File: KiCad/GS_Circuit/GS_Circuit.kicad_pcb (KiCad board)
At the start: 2 copper layers, 88.9 x 76.2 mm, 17 parts, among them J1 AVR-ISP-6, SW1 SW_Push, SW2 SW_SPST, U2 ATtiny85V-10P

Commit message: Loose Saves
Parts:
- BT1: footprint Battery:BatteryHolder_TruPower_BH-331P_3xAA -> GS_Parts:BatteryHolder_Keystone_2464
- C1: value C -> .1 uf
- D1, D2: value LED, TLHG4600, TLHY4600, TLHY4600, TLHF4601 -> LED, QBL8XX60Y Series; footprint LED_THT:LED_D3.0mm -> GS_Parts:LED_D5.0mm
- R1, R2: value R_US -> 91 Ohms
- S1: footprint GS_Parts:TEPT4400 -> GS_Parts:THT_TEPT4400
- moved S1 55.8 mm to (68.2, 26.5)
- moved R4 11.4 mm to (64.4, 40.4)
- moved D2 4.91 mm to (91.9, 60.1)
- moved D1 3.94 mm to (25.8, 60.0)
- moved R3 3.18 mm to (74.5, 34.1)
- moved C1 0.35 mm to (48.1, 26.1)

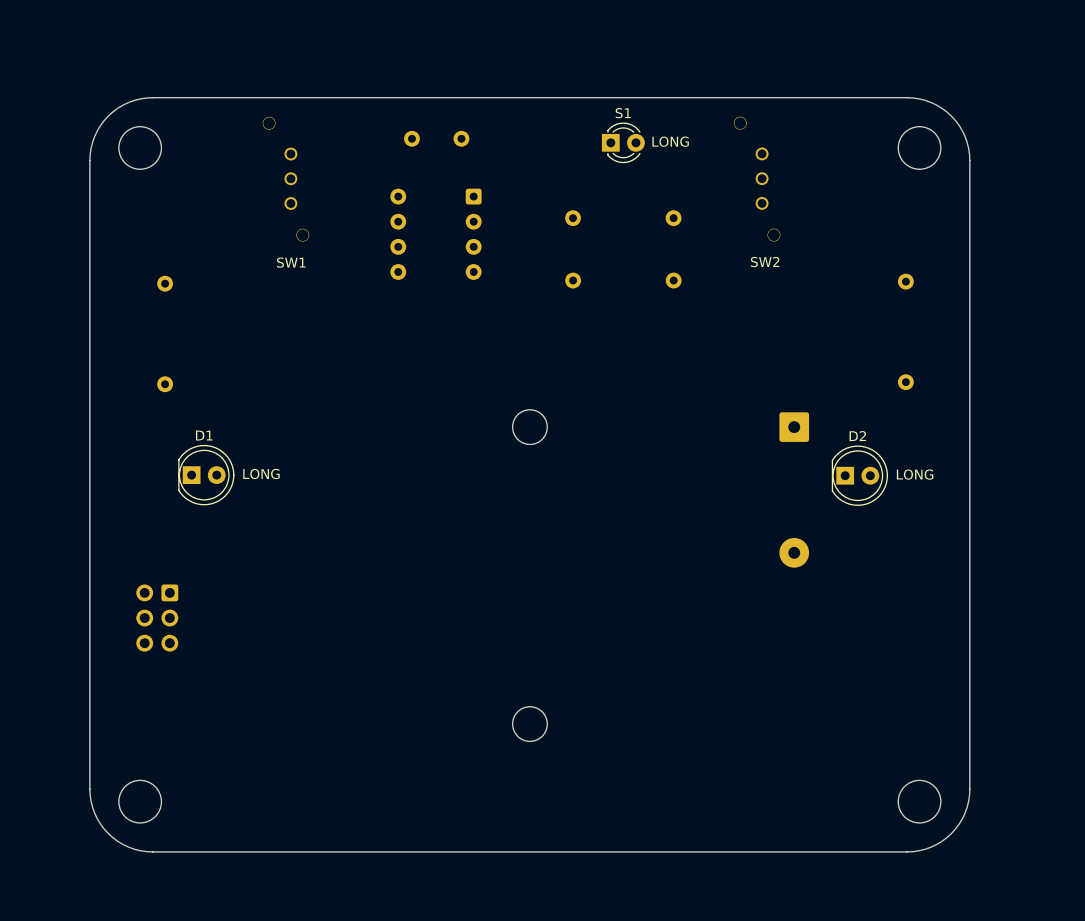
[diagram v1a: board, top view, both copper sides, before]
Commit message: MD E Feeback 3
Moved Lights
Horizontal/Vertical Wiring
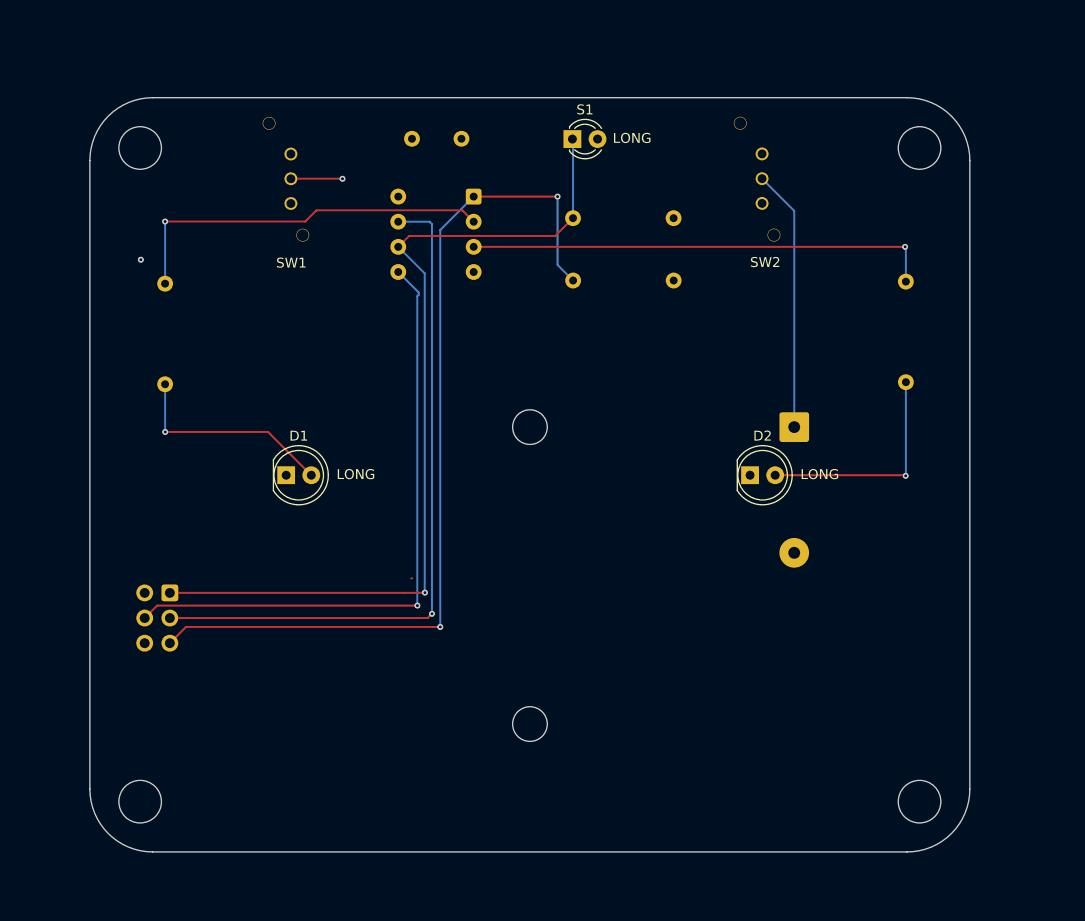
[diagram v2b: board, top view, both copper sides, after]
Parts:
- moved D2 9.62 mm to (82.2, 60.0)
- moved D1 9.55 mm to (35.4, 60.0)
- moved S1 3.90 mm to (64.3, 26.1)
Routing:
- net /~{RST}: track 0.00 -> 90.5 mm, vias 0 -> 2
- net /MISO: track 0.00 -> 88.7 mm, vias 0 -> 1
- net /SCK: track 0.00 -> 69.5 mm, vias 0 -> 1
- net /MOSI: track 0.00 -> 67.9 mm, vias 0 -> 3
- net Net-(U2-XTAL2/PB4): track 0.00 -> 47.1 mm, vias 0 -> 1
- net Net-(U2-XTAL1/PB3): track 0.00 -> 38.6 mm, vias 0 -> 1
- net Net-(BT1-+): track 0.00 -> 26.4 mm
- net Net-(D2-A): track 0.00 -> 22.7 mm, vias 0 -> 1
- net Net-(D1-A): track 0.00 -> 21.4 mm, vias 0 -> 1

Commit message: Wiring
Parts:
- moved R4 6.31 mm to (64.3, 34.1)
- moved R3 6.29 mm to (74.5, 40.4)
- moved R2 5.06 mm to (97.5, 55.7)
- moved R1 4.66 mm to (23.1, 55.5)
- moved D2 1.65 mm to (80.6, 60.0)
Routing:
- net /MOSI: track 67.9 -> 82.9 mm
- net /MISO: track 88.7 -> 96.8 mm
- net /~{RST}: track 90.5 -> 83.8 mm, vias 2 -> 1
- net Net-(D2-A): track 22.7 -> 16.1 mm, vias 1 -> 0
- net Net-(U2-XTAL2/PB4): track 47.1 -> 53.0 mm
- net Net-(D1-A): track 21.4 -> 16.7 mm
- net Net-(U2-XTAL1/PB3): track 38.6 -> 40.9 mm
- added copper zone on B.Cu, net GND
- added copper zone on F.Cu, net VCC
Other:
- board text added: "GS_NIGHT_LIGHT_V1"

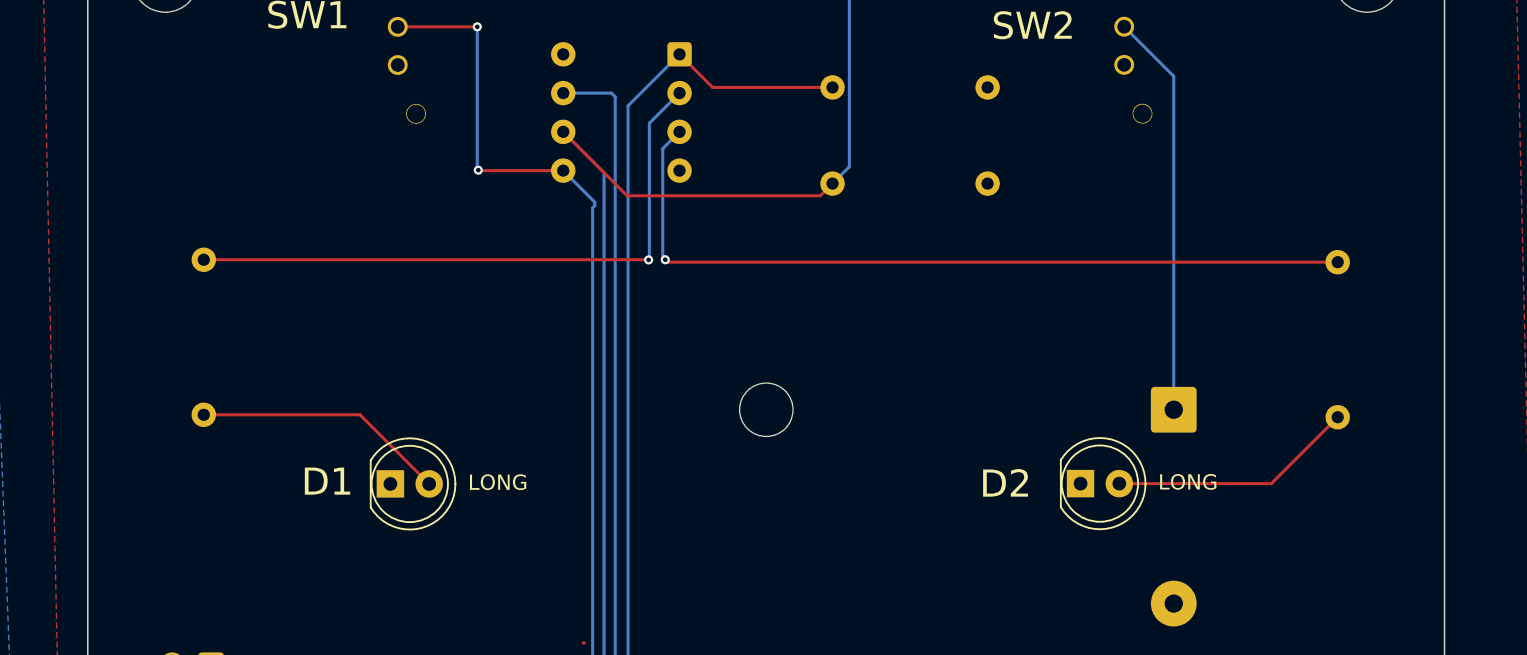
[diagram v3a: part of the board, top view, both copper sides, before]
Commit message: Moved lights to border
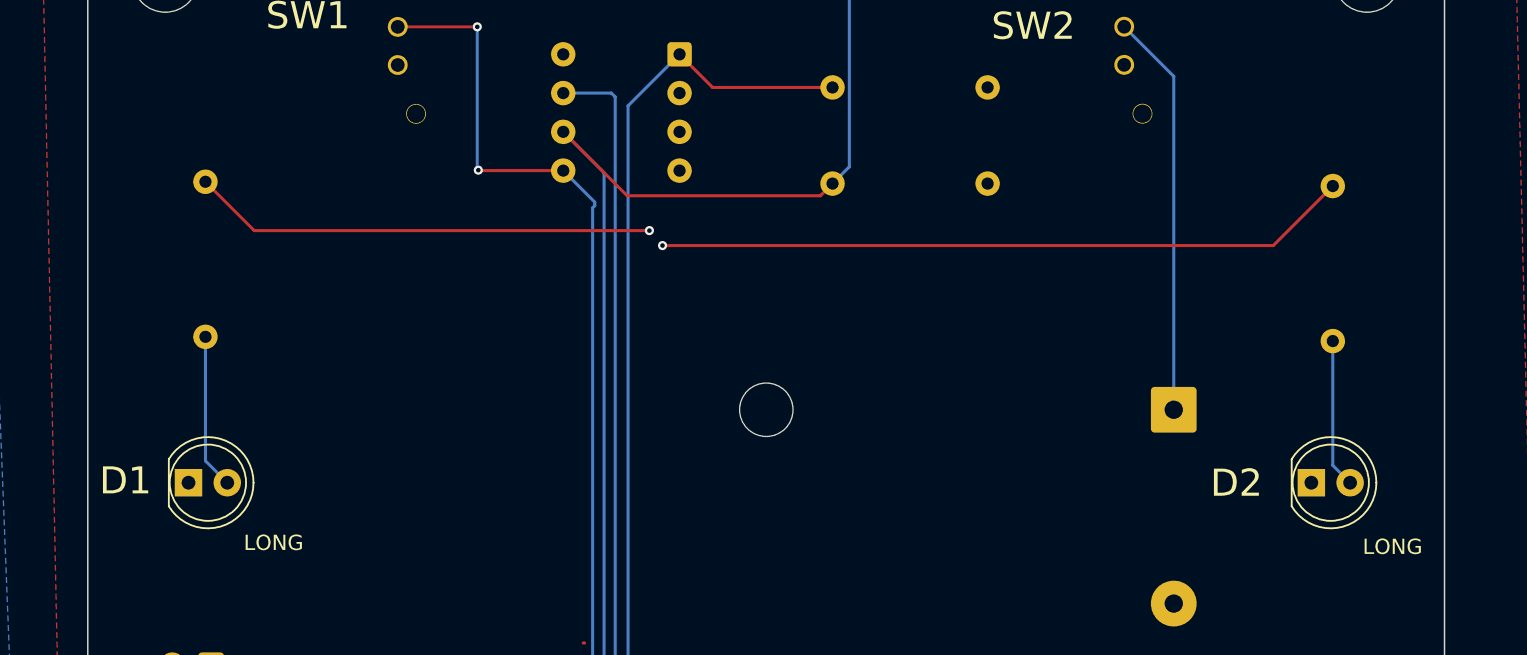
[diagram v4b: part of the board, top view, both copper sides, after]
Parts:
- moved D2 15.1 mm to (95.7, 60.0)
- moved D1 13.2 mm to (22.1, 60.0)
- moved R1 5.11 mm to (23.3, 50.4)
- moved R2 5.00 mm to (97.1, 50.7)
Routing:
- net Net-(U2-XTAL1/PB3): track 40.9 -> 30.4 mm
- net Net-(U2-XTAL2/PB4): track 53.0 -> 45.7 mm
- net Net-(D1-A): track 16.7 -> 10.2 mm, vias 1 -> 0
- net Net-(D2-A): track 16.1 -> 9.75 mm
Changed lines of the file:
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@@
 	(footprint "GS_Parts:LED_D5.0mm"
 		(layer "F.Cu")
-		(at 35.38 60.04)
+		(at 22.15 59.96)
 		(descr "LED, diameter 5.0mm, 2 pins, http://cdn-reichelt.de/documents/datenblatt/A500/LL-504BC2E-009.pdf, generated by kicad-footprint-generator")
 		(tags "LED")
@@
 		)
 		(fp_text user "LONG"
-			(at 5.08 0.508 0)
+			(at 3.61 4.53 0)
 			(unlocked yes)
 			(layer "F.SilkS")
@@
 	(footprint "GS_Parts:LED_D5.0mm"
 		(layer "F.Cu")
-		(at 80.6 60.02)
+		(at 95.725 59.96)
 		(descr "LED, diameter 5.0mm, 2 pins, http://cdn-reichelt.de/documents/datenblatt/A500/LL-504BC2E-009.pdf, generated by kicad-footprint-generator")
 		(tags "LED")
@@
 		)
 		(fp_text user "LONG"
-			(at 5.08 0.508 0)
+			(at 3.355 4.79 0)
 			(unlocked yes)
 			(layer "F.SilkS")
@@
 	(footprint "Resistor_THT:R_Axial_DIN0207_L6.3mm_D2.5mm_P10.16mm_Horizontal"
 		(layer "B.Cu")
-		(at 97.45 55.67 90)
+		(at 97.13 50.68 90)
 		(descr "Resistor, Axial_DIN0207 series, Axial, Horizontal, pin pitch=10.16mm, 0.25W = 1/4W, length*diameter=6.3*2.5mm^2, http://cdn-reichelt.de/documents/datenblatt/B400/1_4W%23YAG.pdf")
 		(tags "Resistor Axial_DIN0207 series Axial Horizontal pin pitch 10.16mm 0.25W = 1/4W length 6.3mm diameter 2.5mm")
@@
 	(footprint "Resistor_THT:R_Axial_DIN0207_L6.3mm_D2.5mm_P10.16mm_Horizontal"
 		(layer "B.Cu")
-		(at 23.15 55.51 90)
+		(at 23.26 50.4 90)
 		(descr "Resistor, Axial_DIN0207 series, Axial, Horizontal, pin pitch=10.16mm, 0.25W = 1/4W, length*diameter=6.3*2.5mm^2, http://cdn-reichelt.de/documents/datenblatt/B400/1_4W%23YAG.pdf")
 		(tags "Resistor Axial_DIN0207 series Axial Horizontal pin pitch 10.16mm 0.25W = 1/4W length 6.3mm diameter 2.5mm")
@@
 	)
 	(segment
-		(start 33.39 55.51)
-		(end 37.92 60.04)
+		(start 23.26 50.4)
+		(end 23.26 58.53)
 		(width 0.2)
-		(layer "F.Cu")
-		(net 4)
-	)
-	(segment
-		(start 23.15 55.51)
-		(end 33.39 55.51)
-		(width 0.2)
-		(layer "F.Cu")
-		(net 4)
-	)
-	(via
-		(at 23.16 55.67)
-		(size 0.6)
-		(drill 0.3)
-		(layers "F.Cu" "B.Cu")
+		(layer "B.Cu")
 		(net 4)
 	)
 	(segment
-		(start 23.15 55.66)
-		(end 23.16 55.67)
+		(start 23.26 58.53)
+		(end 24.69 59.96)
 		(width 0.2)
 		(layer "B.Cu")
@@
 	)
 	(segment
-		(start 52.29 45.35)
-		(end 23.15 45.35)
+		(start 26.46 43.44)
+		(end 52.35 43.44)
 		(width 0.2)
 		(layer "F.Cu")
@@
 	)
 	(segment
-		(start 52.3 45.36)
-		(end 52.29 45.35)
+		(start 23.26 40.24)
+		(end 26.46 43.44)
 		(width 0.2)
 		(layer "F.Cu")
@@
 	)
 	(via
-		(at 52.3 45.36)
+		(at 52.35 43.44)
 		(size 0.6)
 		(drill 0.3)
@@
 	)
 	(segment
-		(start 52.35 36.405)
-		(end 54.325 34.43)
-		(width 0.2)
-		(layer "B.Cu")
-		(net 9)
-	)
-	(segment
-		(start 52.35 45.31)
-		(end 52.35 36.405)
-		(width 0.2)
-		(layer "B.Cu")
-		(net 9)
-	)
-	(segment
-		(start 52.3 45.36)
-		(end 52.35 45.31)
+		(start 93.23 44.42)
+		(end 53.21 44.42)
 		(width 0.2)
-		(layer "B.Cu")
-		(net 9)
+		(layer "F.Cu")
+		(net 10)
 	)
 	(segment
-		(start 53.55 45.51)
-		(end 97.45 45.51)
+		(start 53.21 44.42)
+		(end 53.05 44.42)
 		(width 0.2)
 		(layer "F.Cu")
@@
 	)
 	(segment
-		(start 53.39 45.35)
-		(end 53.55 45.51)
+		(start 97.13 40.52)
+		(end 93.23 44.42)
 		(width 0.2)
 		(layer "F.Cu")
@@
 	)
 	(via
-		(at 53.39 45.35)
+		(at 53.21 44.42)
 		(size 0.6)
 		(drill 0.3)
@@
 	)
 	(segment
-		(start 54.325 36.97)
-		(end 53.224 38.071)
-		(width 0.2)
-		(layer "B.Cu")
-		(net 10)
-	)
-	(segment
-		(start 53.224 38.071)
-		(end 53.224 45.184)
-		(width 0.2)
-		(layer "B.Cu")
-		(net 10)
-	)
-	(segment
-		(start 53.224 45.184)
-		(end 53.39 45.35)
+		(start 97.13 58.825)
+		(end 98.265 59.96)
 		(width 0.2)
 		(layer "B.Cu")
-		(net 10)
-	)
-	(segment
-		(start 97.45 55.67)
-		(end 93.1 60.02)
-		(width 0.2)
-		(layer "F.Cu")
 		(net 11)
 	)
 	(segment
-		(start 93.1 60.02)
-		(end 83.14 60.02)
+		(start 97.13 50.68)
+		(end 97.13 58.825)
 		(width 0.2)
-		(layer "F.Cu")
+		(layer "B.Cu")
 		(net 11)
 	)

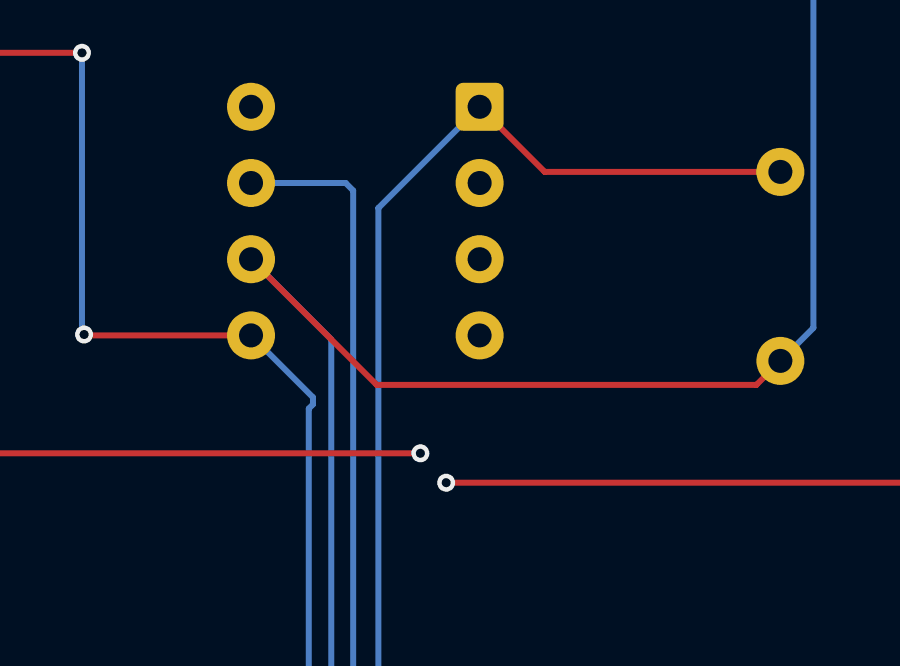
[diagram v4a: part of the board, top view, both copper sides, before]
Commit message: Fixed Connecions for LEDS
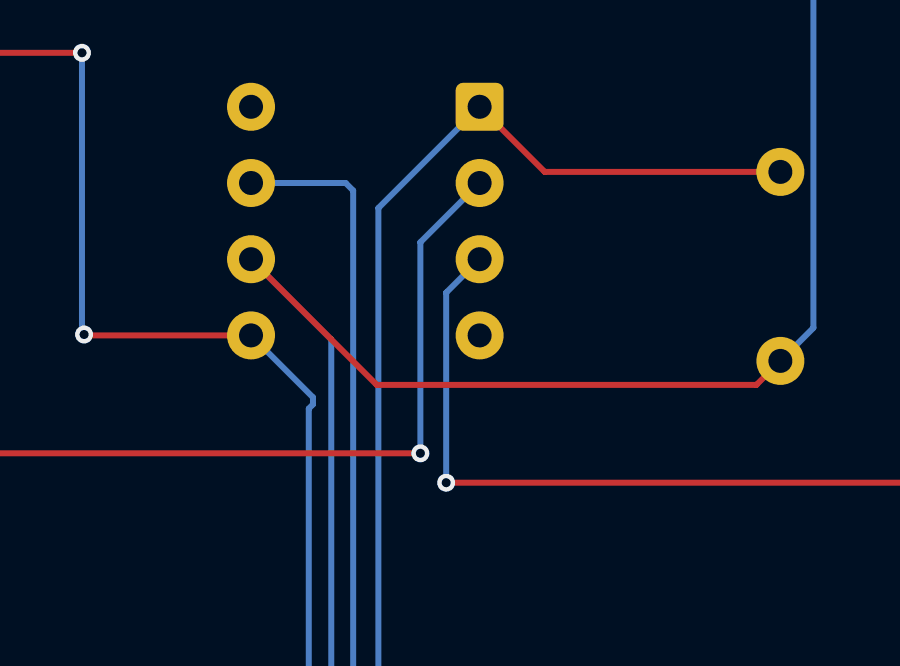
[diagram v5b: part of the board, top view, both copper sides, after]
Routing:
- net Net-(U2-XTAL1/PB3): track 30.4 -> 40.2 mm
- net Net-(U2-XTAL2/PB4): track 45.7 -> 53.6 mm
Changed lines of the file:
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@@
+	)
+	(segment
+		(start 52.35 43.44)
+		(end 52.35 36.405)
+		(width 0.2)
+		(layer "B.Cu")
+		(net 9)
+	)
+	(segment
+		(start 52.35 36.405)
+		(end 54.325 34.43)
+		(width 0.2)
+		(layer "B.Cu")
+		(net 9)
 	)
 	(segment
@@
 		(net 10)
 	)
+	(segment
+		(start 53.21 44.42)
+		(end 53.21 38.085)
+		(width 0.2)
+		(layer "B.Cu")
+		(net 10)
+	)
+	(segment
+		(start 53.21 38.085)
+		(end 54.325 36.97)
+		(width 0.2)
+		(layer "B.Cu")
+		(net 10)
+	)
